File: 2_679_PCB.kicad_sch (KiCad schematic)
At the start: 109 parts, among them J1 POWER_IN, J10 DC Motor Header, J11 DC Motor Header, J12 DC Motor Header, J13 DC Motor Header, J14 Conn_01x06_Female, J15 Conn_01x06_Female, J16 Conn_01x06_Female, J17 Conn_01x06_Female, J18 I2C_3V3, J19 Servo Header, J2 ARDUINO_HEADER_1, J20 Servo Header, J21 Servo Header, J22 Servo Header, J23 Servo Header, J24 Servo Header, J25 Servo Header, J26 Servo Header, J27 RC IN, J28 NEOPIXEL, J29 MPU6050, J3 ARDUINO_HEADER_2, J30 USB_C_Receptacle_USB2.0, J4 I2C_5V, J5 POWER_OUT, J6 DC Motor Header, J7 DC Motor Header, J8 DC Motor Header, J9 DC Motor Header, SW1 SW_SPST, SW2 SW_Push_Open, SW3 SW_P3, SW4 SW_P4, SW5 SW_SPST, U1 SP7652ER-L/TR, U2 AON6558, U3 LMV331, U4 TCA9517DR, U5 AMS1117-5.0, U6 IP2721, U7 BU4SU69G2

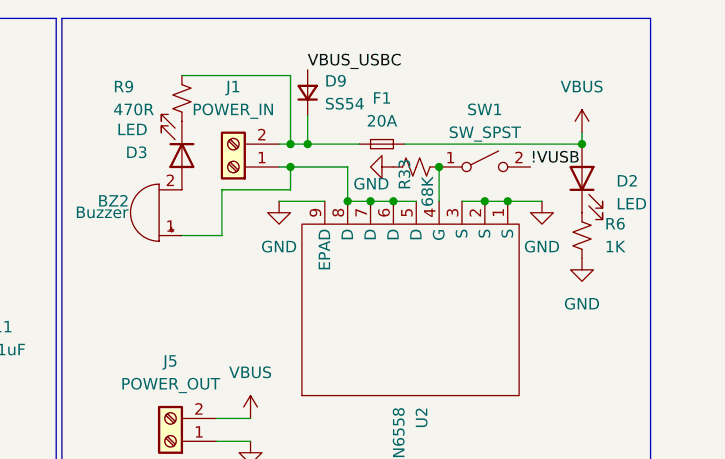
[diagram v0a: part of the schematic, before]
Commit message: fully defined states for inverter
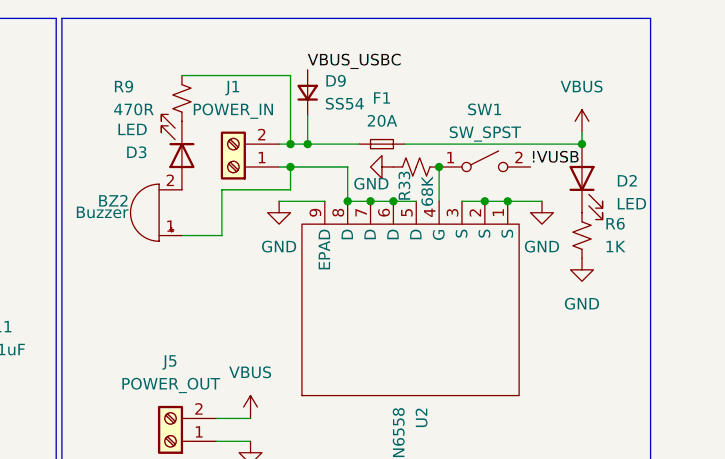
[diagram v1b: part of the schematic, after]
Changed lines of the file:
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@@
   (symbol (lib_id "Device:R_Small_US") (at 258.445 29.21 270) (unit 1)
     (in_bom yes) (on_board yes)
-    (property "Reference" "R33" (id 0) (at 257.175 31.75 0)
+    (property "Reference" "R33" (id 0) (at 257.175 33.02 0)
       (effects (font (size 1.27 1.27)) (justify right))
     )

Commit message: changed e-pads
changed e-pads
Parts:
- R1: value 5.1k -> 5.1R; footprint Resistor_SMD:R_0402_1005Metric -> Resistor_SMD:R_0603_1608Metric; Digikey RMCF0402FT5K10CT-ND -> (none); LCSC C25905 -> C25197
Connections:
- net +5VD: now also D4.1 (VDD), D5.1 (VDD), D6.1 (VDD); no longer D4.4 (VDD), D5.4 (VDD), D6.4 (VDD)
- net D12: now also D4.4 (DIN); no longer D4.3 (DIN)
- net GND: now also D4.3 (VSS), D5.3 (VSS), D6.3 (VSS); no longer D4.2 (VSS), D5.2 (VSS), D6.2 (VSS), U1.28 (EPAD), U1.29 (EPAD), U2.9 (EPAD)
- net LX: now also U1.28 (EPAD)
- net VBUS: now also U1.29 (EPAD)
- new net: D5.2 (DOUT), D6.4 (DIN)
- new net: D4.2 (DOUT), D5.4 (DIN)

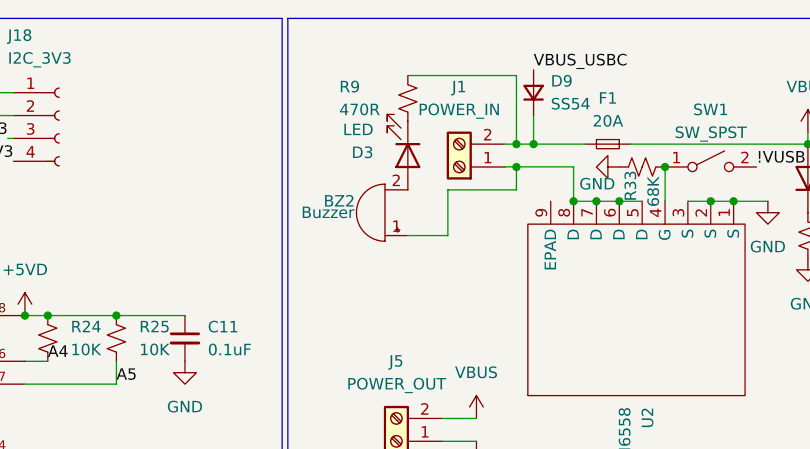
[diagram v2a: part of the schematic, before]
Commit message: fixed DRC
trace was routed incorrectly
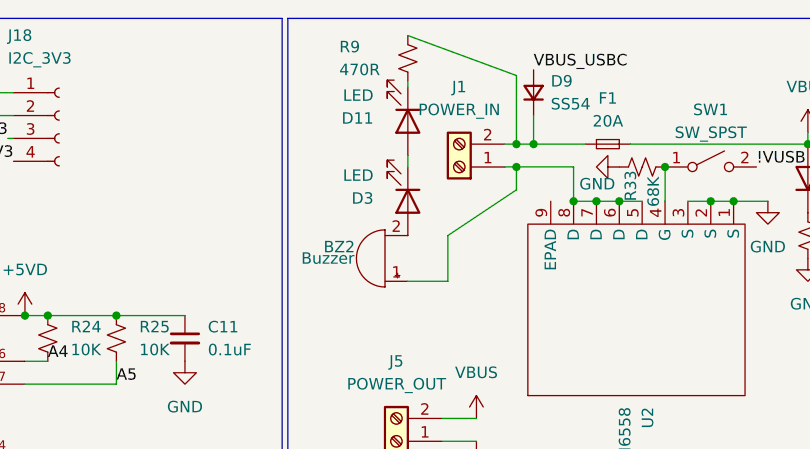
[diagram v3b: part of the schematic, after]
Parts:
- added D11: LED, LED_SMD:LED_0603_1608Metric, symbol Device:LED
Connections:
- net at D3.1 (K): now also D11.2 (A); no longer R9.1
- new net: D11.1 (K), R9.1
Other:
- moved on the sheet: BZ2, D3, R9
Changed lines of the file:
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@@
     (stroke (width 0) (type default) (color 0 0 0 0))
   )
-  (wire (pts (xy 244.475 19.05) (xy 232.41 19.05))
+  (wire (pts (xy 244.475 19.05) (xy 232.41 14.605))
+    (stroke (width 0) (type default) (color 0 0 0 0))
+  )
+  (wire (pts (xy 232.41 19.685) (xy 232.41 20.32))
     (stroke (width 0) (type default) (color 0 0 0 0))
   )
@@
     (stroke (width 0) (type default) (color 0 0 0 0))
   )
-  (wire (pts (xy 236.855 36.83) (xy 236.855 31.75))
+  (wire (pts (xy 236.855 41.91) (xy 236.855 36.83))
     (stroke (width 0) (type default) (color 0 0 0 0))
   )
@@
     (stroke (width 0) (type default) (color 0 0 0 0))
   )
-  (wire (pts (xy 232.41 36.83) (xy 236.855 36.83))
+  (wire (pts (xy 232.41 41.91) (xy 236.855 41.91))
     (stroke (width 0) (type default) (color 0 0 0 0))
   )
@@
     (stroke (width 0) (type default) (color 0 0 0 0))
   )
+  (wire (pts (xy 232.41 27.94) (xy 232.41 29.21))
+    (stroke (width 0) (type default) (color 0 0 0 0))
+  )
   (polyline (pts (xy 13.97 135.89) (xy 83.82 135.89))
     (stroke (width 0) (type default) (color 0 0 0 0))
@@
     (stroke (width 0) (type default) (color 0 0 0 0))
   )
-  (wire (pts (xy 236.855 31.75) (xy 244.475 31.75))
+  (wire (pts (xy 236.855 36.83) (xy 244.475 31.75))
     (stroke (width 0) (type default) (color 0 0 0 0))
   )
@@
     (pin "1")
   )
-  (symbol (lib_id "Device:Buzzer") (at 229.87 34.29 180) (unit 1)
+  (symbol (lib_id "Device:Buzzer") (at 229.87 39.37 180) (unit 1)
     (in_bom yes) (on_board yes)
-    (property "Reference" "BZ2" (id 0) (at 224.79 33.02 0))
-    (property "Value" "Buzzer" (id 1) (at 223.52 34.29 0))
-    (property "Footprint" "Capacitor_THT:CP_Radial_D10.0mm_P5.00mm" (id 2) (at 230.505 36.83 90)
+    (property "Reference" "BZ2" (id 0) (at 224.79 38.1 0))
+    (property "Value" "Buzzer" (id 1) (at 223.52 39.37 0))
+    (property "Footprint" "Capacitor_THT:CP_Radial_D10.0mm_P5.00mm" (id 2) (at 230.505 41.91 90)
       (effects (font (size 1.27 1.27)) hide)
     )
-    (property "Datasheet" "https://www.digikey.com/en/products/detail/pui-audio-inc/AI-1027-TWT-5V-2-R/5011389" (id 3) (at 230.505 36.83 90)
+    (property "Datasheet" "https://www.digikey.com/en/products/detail/pui-audio-inc/AI-1027-TWT-5V-2-R/5011389" (id 3) (at 230.505 41.91 90)
       (effects (font (size 1.27 1.27)) hide)
     )
-    (property "Digikey" "668-1454-ND" (id 4) (at 229.87 34.29 0)
+    (property "Digikey" "668-1454-ND" (id 4) (at 229.87 39.37 0)
       (effects (font (size 1.27 1.27)) hide)
     )
@@
     (pin "3")
   )
-  (symbol (lib_id "Device:LED") (at 232.41 27.94 270) (unit 1)
+  (symbol (lib_id "Device:LED") (at 232.41 33.02 270) (unit 1)
     (in_bom yes) (on_board yes) (fields_autoplaced)
-    (property "Reference" "D3" (id 0) (at 228.6 27.6226 90)
+    (property "Reference" "D3" (id 0) (at 228.6 32.7026 90)
       (effects (font (size 1.27 1.27)) (justify right))
     )
-    (property "Value" "LED" (id 1) (at 228.6 25.0826 90)
+    (property "Value" "LED" (id 1) (at 228.6 30.1626 90)
       (effects (font (size 1.27 1.27)) (justify right))
     )
-    (property "Footprint" "LED_SMD:LED_0603_1608Metric" (id 2) (at 232.41 27.94 0)
+    (property "Footprint" "LED_SMD:LED_0603_1608Metric" (id 2) (at 232.41 33.02 0)
       (effects (font (size 1.27 1.27)) hide)
     )
-    (property "Datasheet" "" (id 3) (at 232.41 27.94 0)
+    (property "Datasheet" "" (id 3) (at 232.41 33.02 0)
       (effects (font (size 1.27 1.27)) hide)
     )
-    (property "Digikey" "" (id 4) (at 232.41 27.94 0)
+    (property "Digikey" "" (id 4) (at 232.41 33.02 0)
       (effects (font (size 1.27 1.27)) hide)
     )
-    (property "LCSC" "C2286" (id 5) (at 232.41 27.94 0)
+    (property "LCSC" "C2286" (id 5) (at 232.41 33.02 0)
       (effects (font (size 1.27 1.27)) hide)
     )
@@
     (pin "1")
   )
+  (symbol (lib_id "Device:LED") (at 232.41 24.13 270) (unit 1)
+    (in_bom yes) (on_board yes) (fields_autoplaced)
+    (property "Reference" "D11" (id 0) (at 228.6 23.8126 90)
+      (effects (font (size 1.27 1.27)) (justify right))
+    )
+    (property "Value" "LED" (id 1) (at 228.6 21.2726 90)
+      (effects (font (size 1.27 1.27)) (justify right))
+    )
+    (property "Footprint" "LED_SMD:LED_0603_1608Metric" (id 2) (at 232.41 24.13 0)
+      (effects (font (size 1.27 1.27)) hide)
+    )
+    (property "Datasheet" "" (id 3) (at 232.41 24.13 0)
+      (effects (font (size 1.27 1.27)) hide)
+    )
+    (property "Digikey" "" (id 4) (at 232.41 24.13 0)
+      (effects (font (size 1.27 1.27)) hide)
+    )
+    (property "LCSC" "C2286" (id 5) (at 232.41 24.13 0)
+      (effects (font (size 1.27 1.27)) hide)
+    )
+    (pin "1")
+    (pin "2")
+  )
   (symbol (lib_id "Device:R_Small_US") (at 58.42 110.49 0) (unit 1)
     (in_bom yes) (on_board yes) (fields_autoplaced)
@@
     (pin "1")
   )
-  (symbol (lib_id "Device:R_Small_US") (at 232.41 21.59 180) (unit 1)
+  (symbol (lib_id "Device:R_Small_US") (at 232.41 17.145 180) (unit 1)
     (in_bom yes) (on_board yes)
-    (property "Reference" "R9" (id 0) (at 224.79 20.32 0)
+    (property "Reference" "R9" (id 0) (at 224.79 15.875 0)
       (effects (font (size 1.27 1.27)) (justify right))
     )
-    (property "Value" "470R" (id 1) (at 224.79 22.86 0)
+    (property "Value" "470R" (id 1) (at 224.79 18.415 0)
       (effects (font (size 1.27 1.27)) (justify right))
     )
-    (property "Footprint" "Resistor_SMD:R_0402_1005Metric" (id 2) (at 232.41 21.59 0)
+    (property "Footprint" "Resistor_SMD:R_0402_1005Metric" (id 2) (at 232.41 17.145 0)
       (effects (font (size 1.27 1.27)) hide)
     )
-    (property "Datasheet" "https://www.digikey.com/en/products/detail/stackpole-electronics-inc/RMCF0402FT1K00/1761754" (id 3) (at 232.41 21.59 0)
+    (property "Datasheet" "https://www.digikey.com/en/products/detail/stackpole-electronics-inc/RMCF0402FT1K00/1761754" (id 3) (at 232.41 17.145 0)
       (effects (font (size 1.27 1.27)) hide)
     )
-    (property "Digikey" "RMCF0402FT1K00CT-ND" (id 4) (at 232.41 21.59 0)
+    (property "Digikey" "RMCF0402FT1K00CT-ND" (id 4) (at 232.41 17.145 0)
       (effects (font (size 1.27 1.27)) hide)
     )
-    (property "LCSC" "C25117" (id 5) (at 232.41 21.59 0)
+    (property "LCSC" "C25117" (id 5) (at 232.41 17.145 0)
       (effects (font (size 1.27 1.27)) hide)
     )
@@
       (reference "D10") (unit 1) (value "1N5819WS") (footprint "Diode_SMD:D_SOD-323")
     )
+    (path "/e6ba9bbf-fa40-423b-8fc4-e4da3a241f8e"
+      (reference "D11") (unit 1) (value "LED") (footprint "LED_SMD:LED_0603_1608Metric")
+    )
     (path "/bed1d504-b033-4b90-9ded-9efc8c2e98f6"

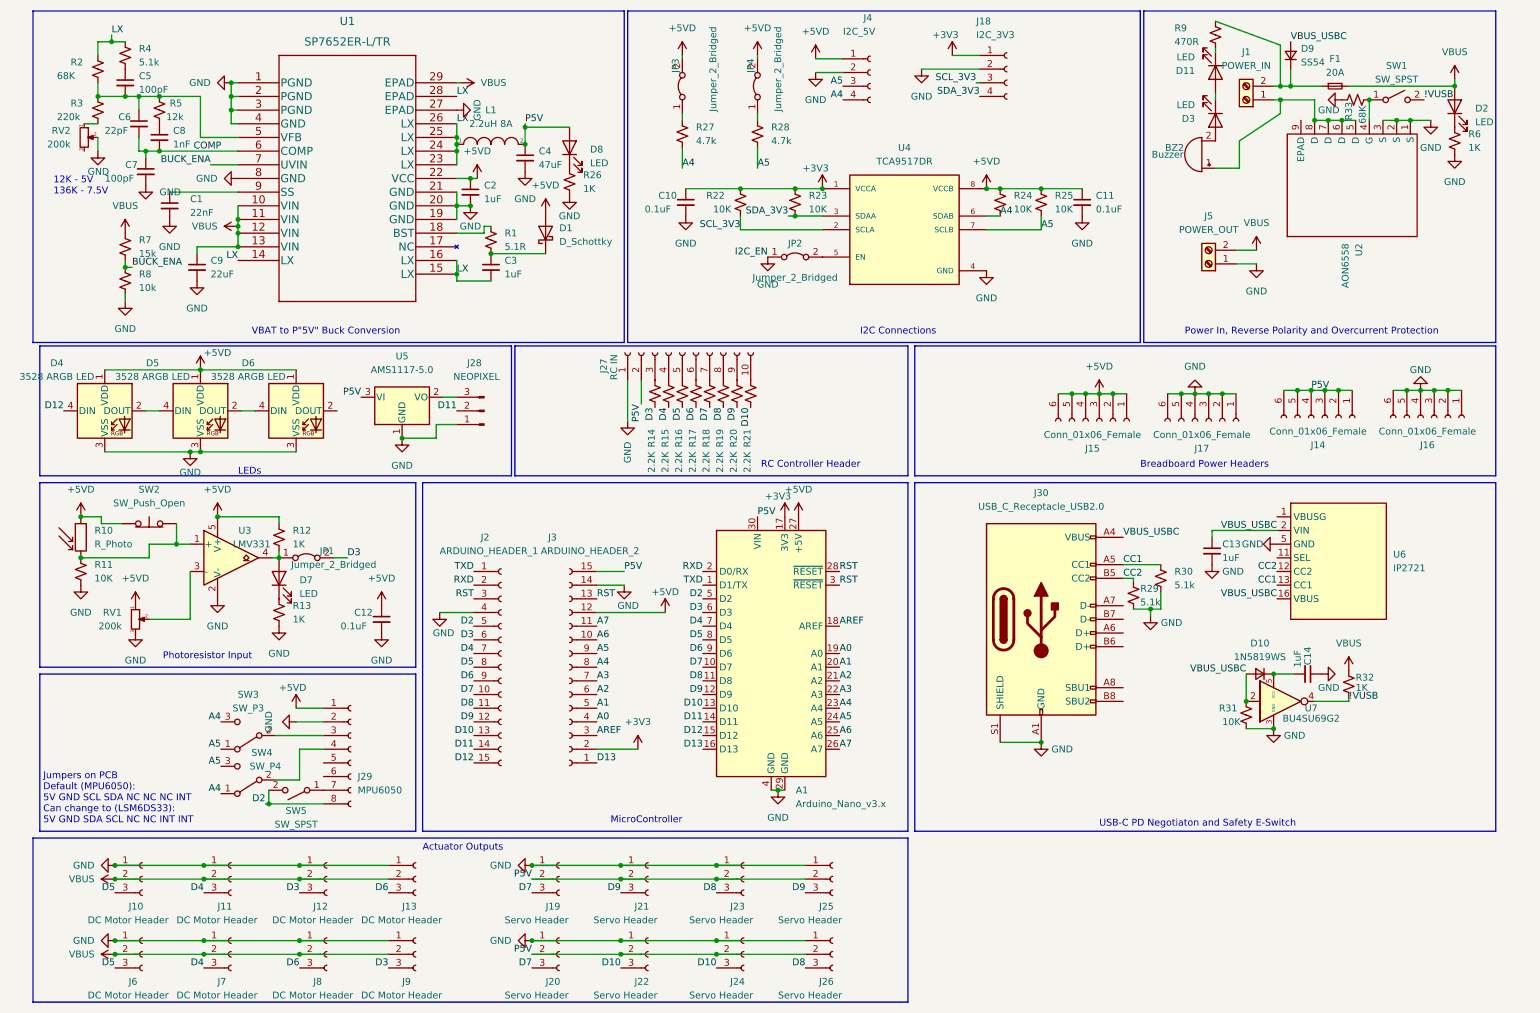
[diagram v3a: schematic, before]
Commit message: added breakout boards
Added boards to increase space use of the board to 4x4"
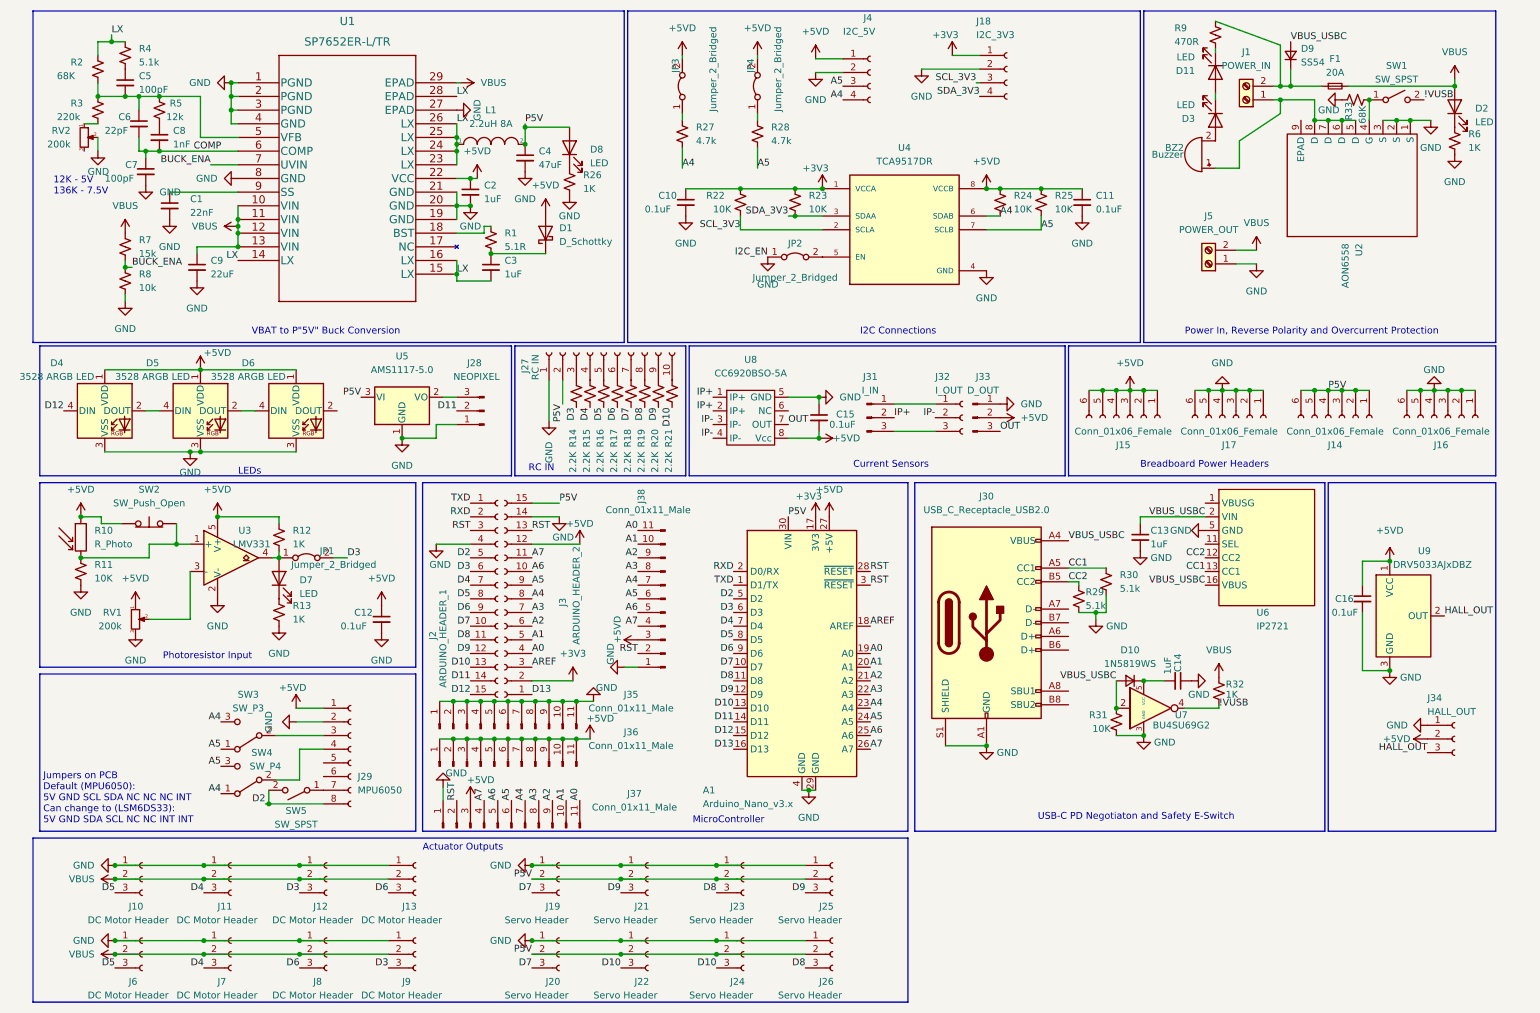
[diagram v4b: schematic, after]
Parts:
- added C15, C16: 0.1uF, Capacitor_SMD:C_0402_1005Metric, symbol Device:C_Small
- added J31: I_IN, Connector_PinSocket_2.54mm:PinSocket_1x03_P2.54mm_Vertical, symbol Connector:Conn_01x03_Male
- added J32: I_OUT, Connector_PinSocket_2.54mm:PinSocket_1x03_P2.54mm_Vertical, symbol Connector:Conn_01x03_Female
- added J33: D_OUT, Connector_PinSocket_2.54mm:PinSocket_1x03_P2.54mm_Vertical, symbol Connector:Conn_01x03_Male
- added J34: HALL_OUT, Connector_PinHeader_2.54mm:PinHeader_1x03_P2.54mm_Vertical_SMD_Pin1Left, symbol Connector:Conn_01x03_Female
- added J35, J36, J37, J38: Conn_01x11_Male, Connector_PinHeader_2.54mm:PinHeader_1x11_P2.54mm_Vertical, symbol Connector:Conn_01x11_Male
- added U8: CC6920BSO-5A, Package_SO:SOP-8_3.9x4.9mm_P1.27mm, symbol CC6920BSO-5A:CC6920BSO-5A
- added U9: DRV5033AJxDBZ, Package_TO_SOT_SMD:SOT-23, symbol Sensor_Magnetic:DRV5033AJxDBZ
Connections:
- net +5VD: now also C15.2, C16.1, J33.2 (Pin_2), J34.2 (Pin_2), J36.1 (Pin_1), J36.10 (Pin_10), J36.11 (Pin_11), J36.2 (Pin_2), J36.3 (Pin_3), J36.4 (Pin_4), J36.5 (Pin_5), J36.6 (Pin_6), J36.7 (Pin_7), J36.8 (Pin_8), J36.9 (Pin_9), J37.3 (Pin_3), J38.3 (Pin_3), U8.8 (Vcc), U9.1 (VCC)
- net A0: now also J37.11 (Pin_11), J38.11 (Pin_11)
- net A1: now also J37.10 (Pin_10), J38.10 (Pin_10)
- net A2: now also J37.9 (Pin_9), J38.9 (Pin_9)
- net A3: now also J37.8 (Pin_8), J38.8 (Pin_8)
- net A4: now also J37.7 (Pin_7), J38.7 (Pin_7)
- net A5: now also J37.6 (Pin_6), J38.6 (Pin_6)
- net A6: now also J37.5 (Pin_5), J38.5 (Pin_5)
- net A7: now also J37.4 (Pin_4), J38.4 (Pin_4)
- net GND: now also C15.1, C16.2, J33.1 (Pin_1), J34.1 (Pin_1), J35.1 (Pin_1), J35.10 (Pin_10), J35.11 (Pin_11), J35.2 (Pin_2), J35.3 (Pin_3), J35.4 (Pin_4), J35.5 (Pin_5), J35.6 (Pin_6), J35.7 (Pin_7), J35.8 (Pin_8), J35.9 (Pin_9), J37.1 (Pin_1), J38.1 (Pin_1), U8.5 (GND), U9.3 (GND)
- net RST: now also J37.2 (Pin_2), J38.2 (Pin_2)
- new net: J31.1 (Pin_1), J32.1 (Pin_1)
- new net: J31.3 (Pin_3), J32.3 (Pin_3)
- new net HALL_OUT: J34.3 (Pin_3), U9.2 (OUT)
- new net IP+: J31.2 (Pin_2), U8.1 (IP+), U8.2 (IP+)
- new net IP-: J32.2 (Pin_2), U8.3 (IP-), U8.4 (IP-)
- new net OUT: J33.3 (Pin_3), U8.7 (OUT)
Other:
- note added: "Current Sensors"
- note added: "RC IN"
- note removed: "RC Controller Header"
- moved on the sheet: A1, C13, C14, D10, J14, J15, J16, J17, J2, J27, J3, J30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

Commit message: updated BOM
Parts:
- A1: Digikey (none) -> 1738-1026-ND
- C1: Digikey 399-C0402C223K5REC7411CT-ND -> (none)
- C10, C11, C12, C15, C16: Digikey 490-3160-1-ND -> (none)
- C13, C14, C2, C3: Digikey 1276-1067-1-ND -> (none)
- C5, C7: Digikey 311-1024-1-ND -> (none)
- C6: Digikey 311-1018-1-ND -> (none)
- C8: Digikey 399-C0402C102J1GEC7411CT-ND -> (none)
- J29: Digikey (none) -> S7006-ND
- J31, J32, J33: Digikey (none) -> S7036-ND
- J34: Digikey (none) -> S5595-ND
- J35, J36, J37, J38: Digikey (none) -> S7009-ND
- R11, R22, R23, R24, R25, R31, R8: Digikey RMCF0402FT10K0CT-ND -> (none)
- R12, R13, R26, R32, R6, R9: Digikey RMCF0402FT1K00CT-ND -> (none)
- R14, R15, R16, R17, R18, R19, R20, R21: Digikey RMCF0402FT2K20CT-ND -> (none)
- R2, R33: Digikey RMCF0402FT68K1CT-ND -> (none)
- R27, R28: Digikey 311-4.7KLRCT-ND -> (none)
- R29, R30, R4: Digikey RMCF0402FT5K10CT-ND -> (none)
- R3: Digikey P232KLCT-ND -> (none)
- R5: Digikey 311-12.0KLRCT-ND -> (none)
- R7: Digikey RMCF0402FT15K0CT-ND -> (none)
- RV1, RV2: LCSC C25764 -> (none)
- U5: Digikey ZLDO1117G50DICT-ND -> (none)

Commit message: added usb-c digikey part number
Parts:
- J30: Digikey (none) -> 2073-USB4105-GF-ACT-ND
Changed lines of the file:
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@@
+      (effects (font (size 1.27 1.27)) hide)
+    )
+    (property "Digikey" "2073-USB4105-GF-ACT-ND" (id 4) (at 189.865 126.365 0)
       (effects (font (size 1.27 1.27)) hide)
     )
